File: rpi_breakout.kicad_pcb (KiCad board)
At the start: 2 copper layers, 65 x 30 mm, 31 parts, among them J1 R22, J11 R22, J14 Raspberry_Pi_2_3, J17 Raspberry_Pi_2_3, J18 R22, J19 R22, J3 R22, J5 R22, J7 R22, J9 R22

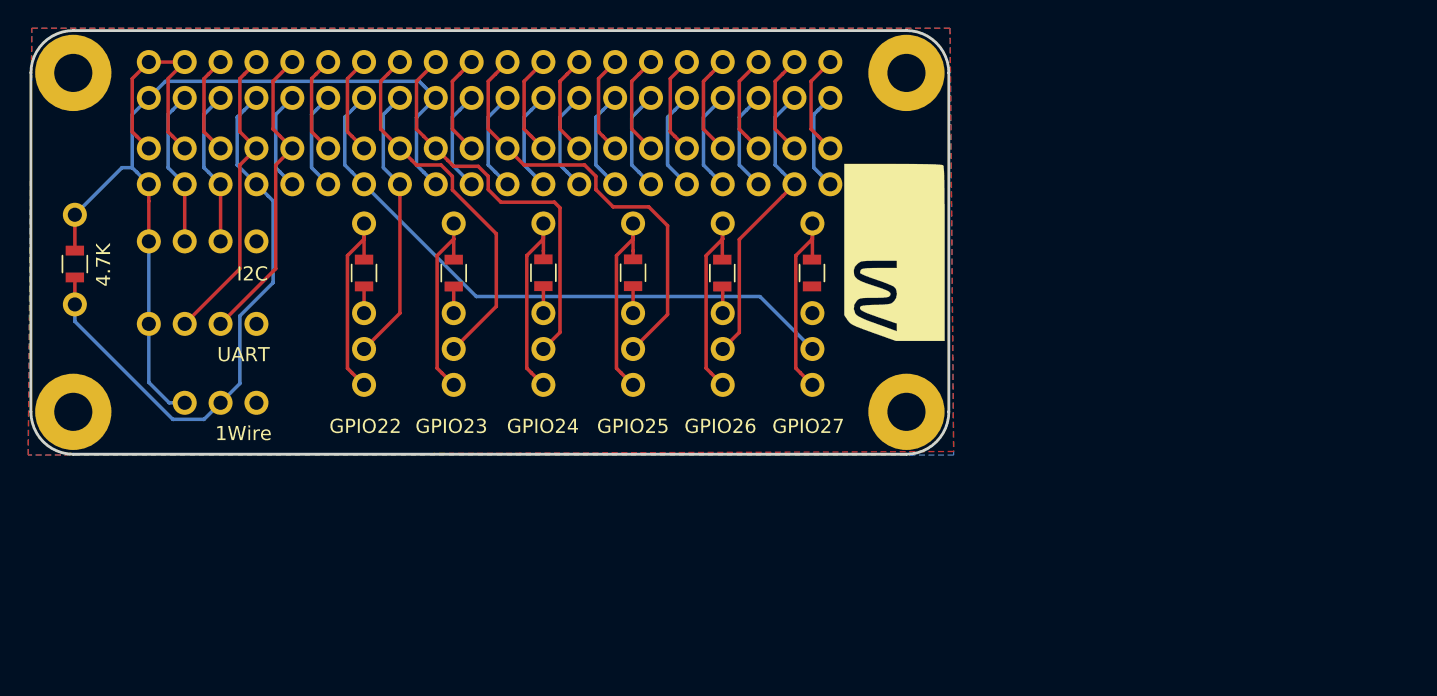
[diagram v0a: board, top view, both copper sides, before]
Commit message: Fix corner mounting holes, increase spacing b/w headers. Tag 1.1
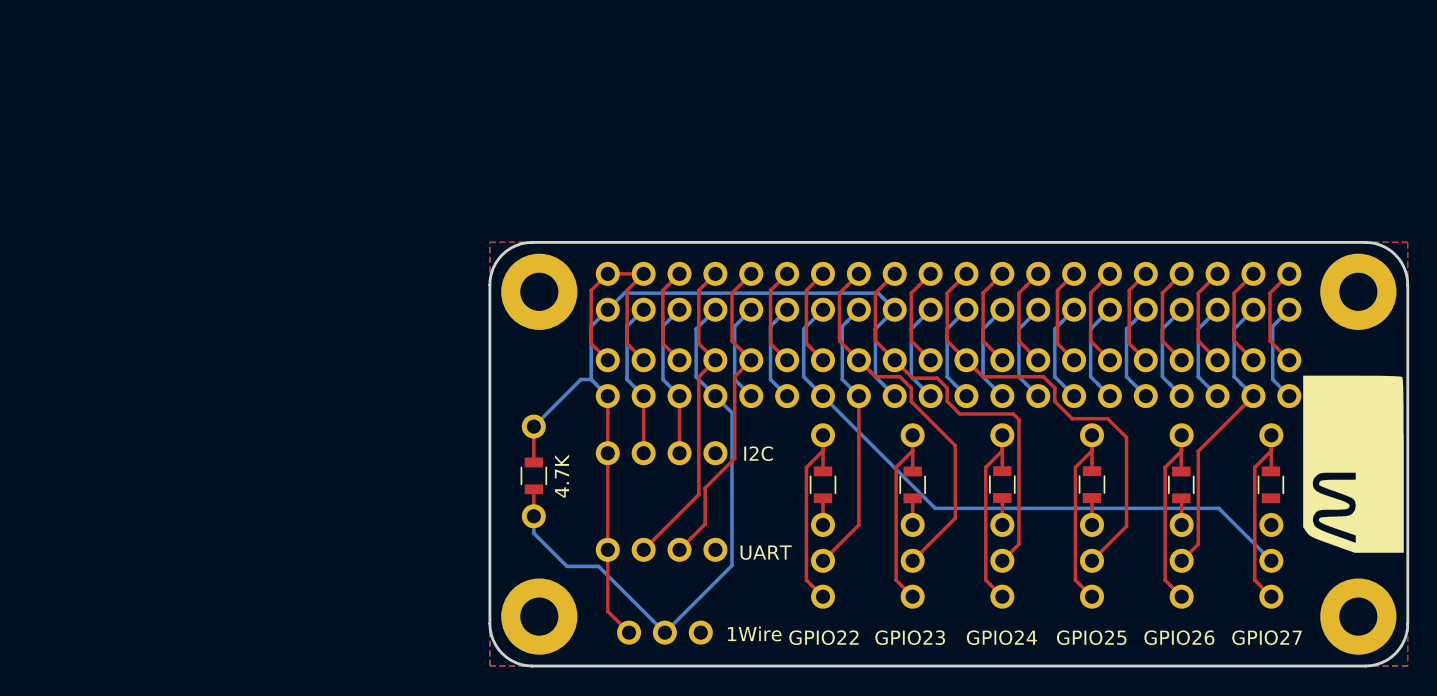
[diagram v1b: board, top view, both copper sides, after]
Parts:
- REF**: moved to B.Cu
- moved REF** 36.5 mm to (103.5, 103.5)
- moved UART 36.2 mm to (108.3, 121.8)
- moved REF** 36.0 mm to (103.5, 126.5)
- moved GPIO26 35.8 mm to (149.0, 120.0)
- moved J5 35.8 mm to (149.0, 113.7)
- moved 4.7K 35.8 mm to (103.1, 116.5)
- moved G*** 35.8 mm to (161.2, 115.7)
- moved GPIO22 35.8 mm to (123.6, 120.0)
- moved GPIO23 35.8 mm to (129.9, 120.0)
- moved GPIO27 35.8 mm to (155.3, 120.0)
- moved I2C 35.8 mm to (108.3, 114.9)
- moved J1 35.8 mm to (123.6, 113.7)
- moved J11 35.8 mm to (155.3, 113.7)
- moved J14 35.8 mm to (108.3, 104.8)
- moved J17 35.8 mm to (108.3, 110.9)
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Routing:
- net 8: track 21.6 -> 22.6 mm
- net 10: track 21.8 -> 22.8 mm
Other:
- board text added: "v1.1"
- board text removed: "v1.0"
